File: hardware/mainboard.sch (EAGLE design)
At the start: 84 parts, among them IC1 ATMEGA328, IC10 HM628512A_DIL32, IC11 HM628512A_DIL32, IC12 7805TV, IC13 DS1210-8PDIP, IC14 6N138, IC3 TLC074, IC4 74HCT04N, IC5 74HC238N, IC6 74HCT573N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

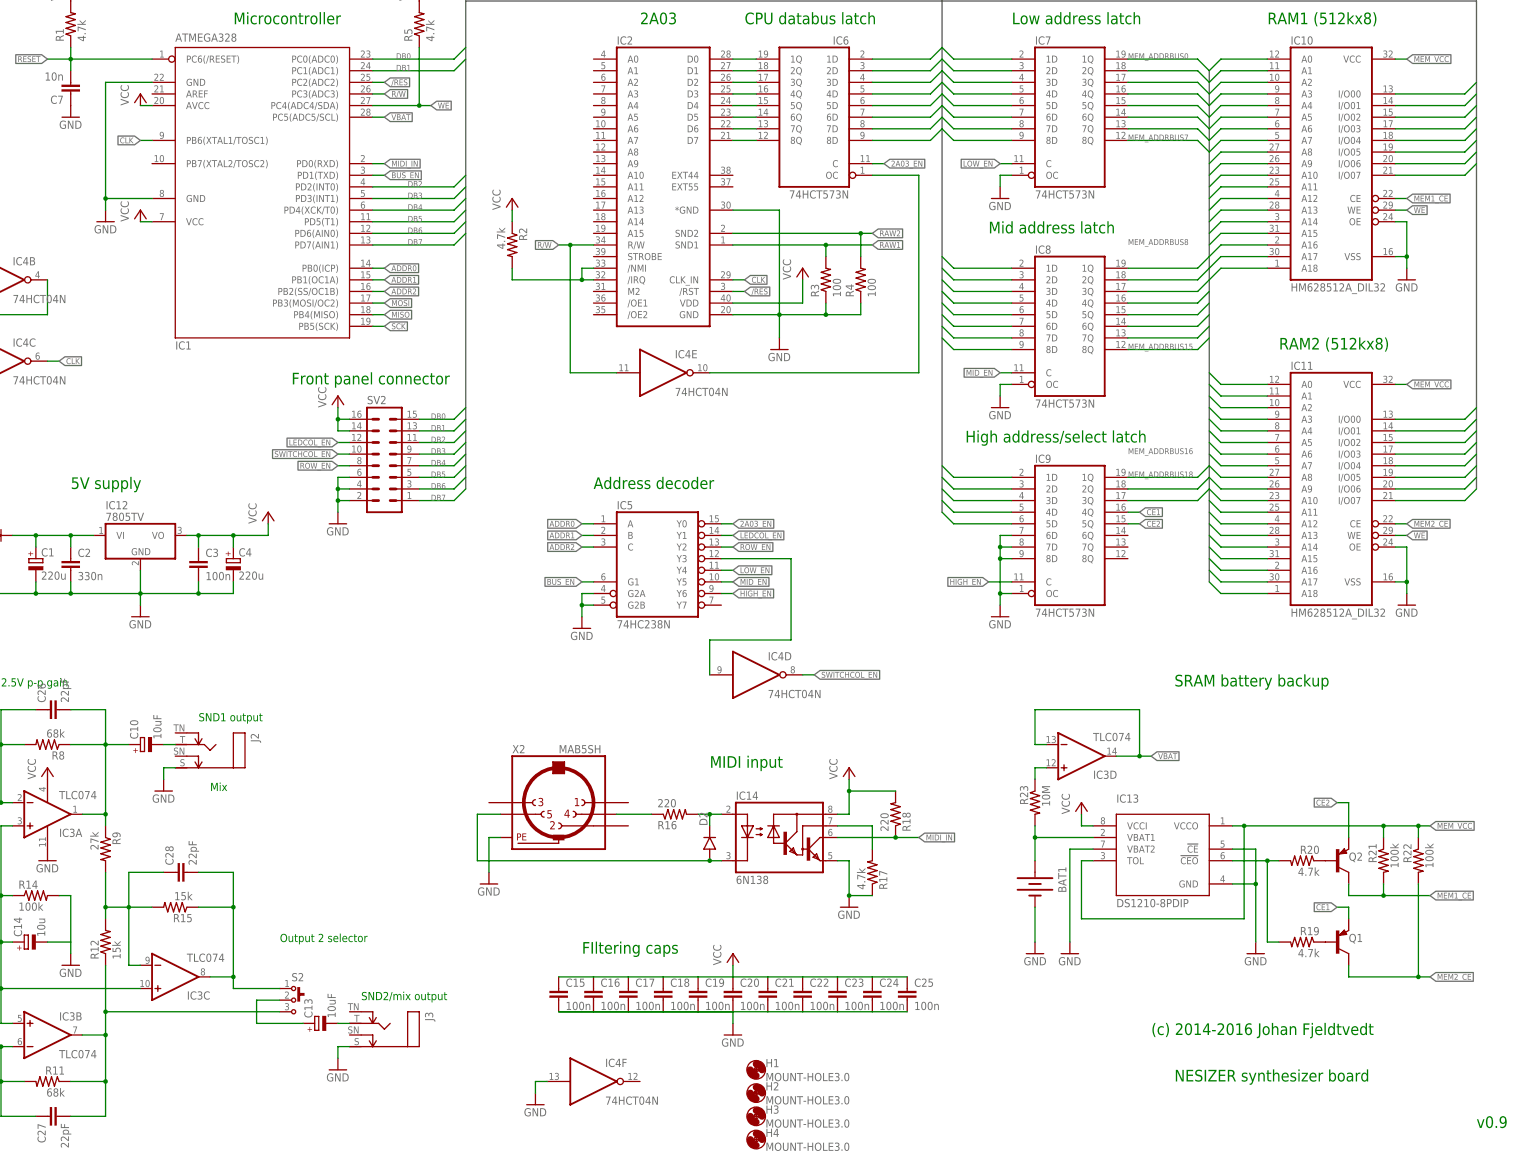
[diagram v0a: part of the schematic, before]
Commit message: mainboard v0.95: fixes and MIDI out
Fixed faults with battery measurement and RESET circuitry.

Added MIDI OUT connector.
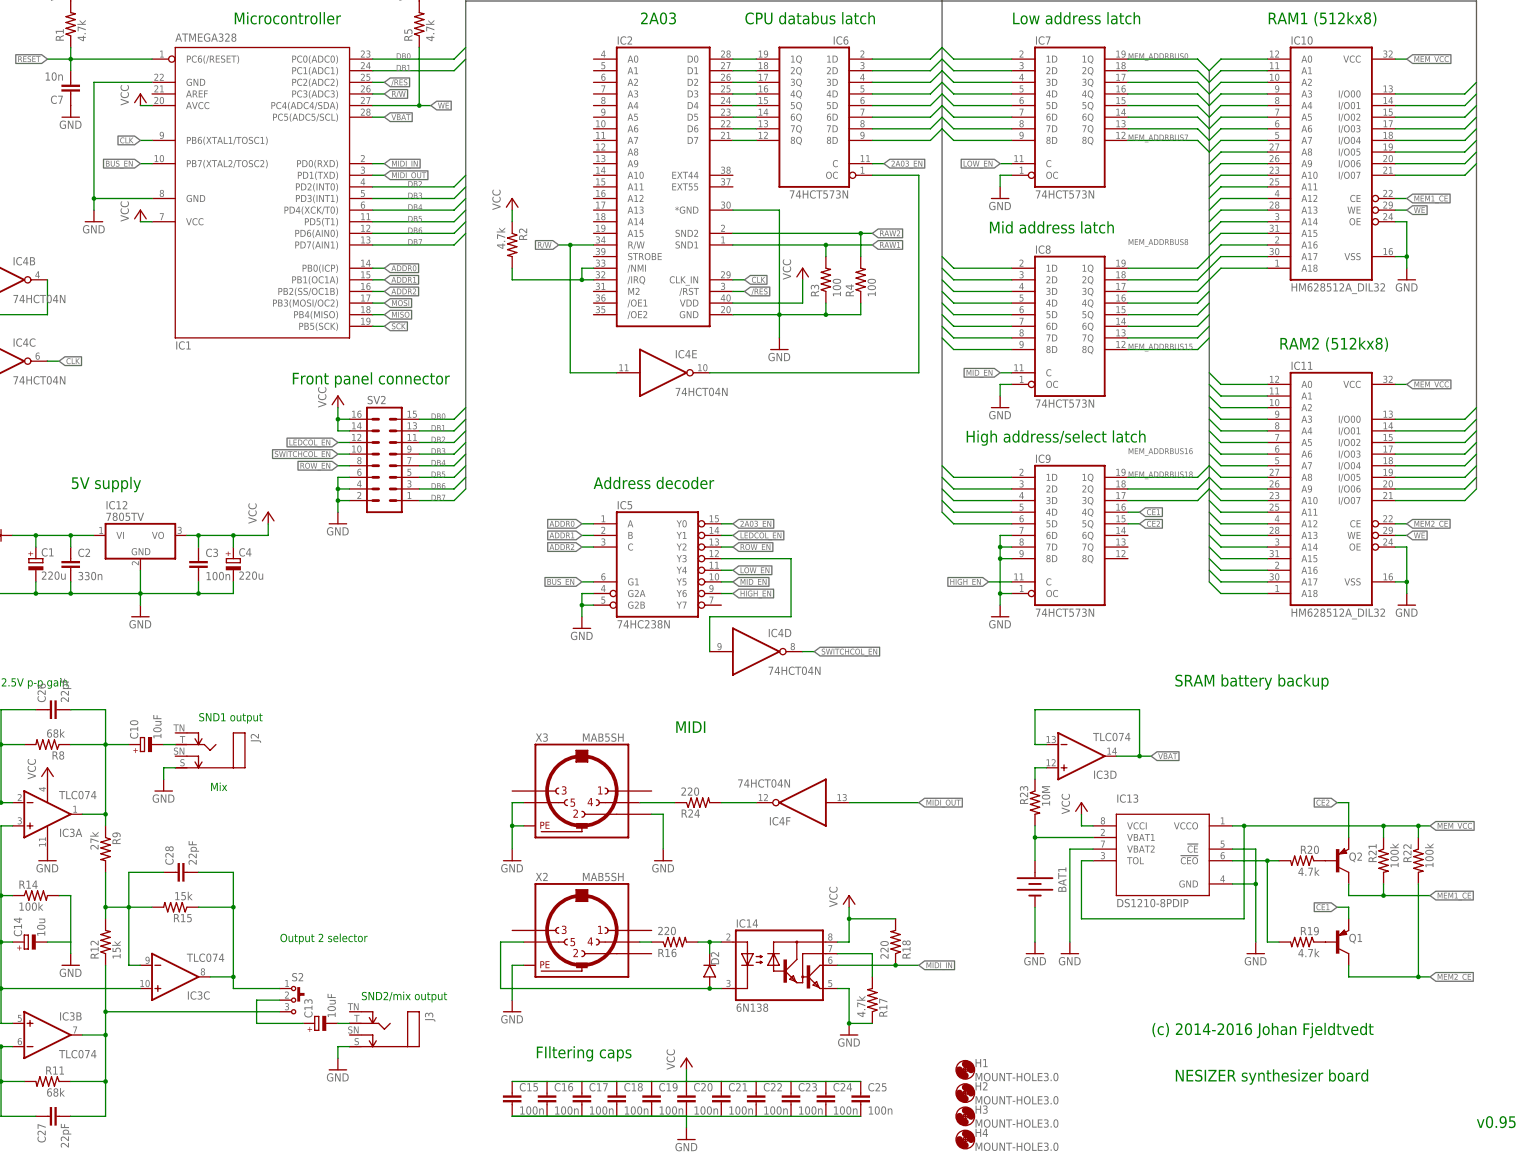
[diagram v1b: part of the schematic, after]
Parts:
- added R24: 220, rcl:R-US_0207/7
- added X3: MAB5SH, con-hirschmann:MAB5SH
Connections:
- new net MIDI_OUT: IC1.PD1(TXD), IC4F.I
- new net N$40: IC4F.O, R24.2
- new net N$41: R24.1, X3.4
- net BUS_EN: now also IC1.PB7(XTAL2/TOSC2); no longer IC1.PD1(TXD)
- net GND: now also X3.2, X3.5, X3.PE; no longer IC4F.I
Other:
- note added: "MIDI"
- note added: "v0.95"
- note removed: "MIDI input"
- note removed: "v0.9"
- moved on the sheet: C15, C16, C17, C18, C19, C20, C21, C22, C23, C24, C25, D2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

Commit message: add 220 resistor to MIDI out
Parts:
- added R25: 220, rcl:R-US_0207/7
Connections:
- new net N$42: R25.1, X3.5
- net GND: now also R25.2; no longer X3.5
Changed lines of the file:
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@@
 <part name="R24" library="rcl" deviceset="R-US_" device="0207/7" value="220"/>
 <part name="GND17" library="supply1" deviceset="GND" device=""/>
+<part name="R25" library="rcl" deviceset="R-US_" device="0207/7" value="220"/>
+<part name="GND28" library="supply1" deviceset="GND" device=""/>
 </parts>
 <sheets>
@@
 <instance part="R24" gate="G$1" x="129.54" y="-81.28" rot="MR180"/>
 <instance part="GND17" gate="1" x="88.9" y="-93.98"/>
+<instance part="R25" gate="G$1" x="83.82" y="-81.28" rot="MR0"/>
+<instance part="GND28" gate="1" x="76.2" y="-93.98"/>
 </instances>
 <busses>
@@
 </segment>
 <segment>
-<pinref part="X3" gate="G$1" pin="5"/>
-<wire x1="91.44" y1="-81.28" x2="88.9" y2="-81.28" width="0.1524" layer="91"/>
-<wire x1="88.9" y1="-81.28" x2="88.9" y2="-86.36" width="0.1524" layer="91"/>
 <pinref part="GND17" gate="1" pin="GND"/>
 <pinref part="X3" gate="G$1" pin="PE"/>
 <wire x1="88.9" y1="-86.36" x2="88.9" y2="-91.44" width="0.1524" layer="91"/>
 <wire x1="91.44" y1="-86.36" x2="88.9" y2="-86.36" width="0.1524" layer="91"/>
-<junction x="88.9" y="-86.36"/>
+</segment>
+<segment>
+<pinref part="R25" gate="G$1" pin="2"/>
+<wire x1="78.74" y1="-81.28" x2="76.2" y2="-81.28" width="0.1524" layer="91"/>
+<wire x1="76.2" y1="-81.28" x2="76.2" y2="-91.44" width="0.1524" layer="91"/>
+<pinref part="GND28" gate="1" pin="GND"/>
 </segment>
 </net>
@@
 </segment>
 </net>
+<net name="N$42" class="0">
+<segment>
+<pinref part="X3" gate="G$1" pin="5"/>
+<wire x1="91.44" y1="-81.28" x2="88.9" y2="-81.28" width="0.1524" layer="91"/>
+<pinref part="R25" gate="G$1" pin="1"/>
+</segment>
+</net>
